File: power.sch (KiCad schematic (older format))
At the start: 5 parts, among them U301 MCP1754ST-3302E/MB

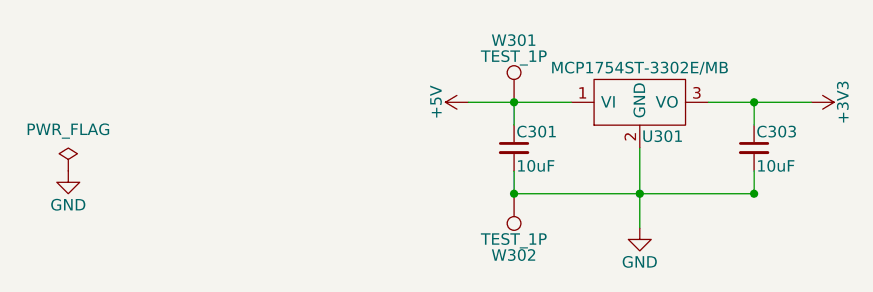
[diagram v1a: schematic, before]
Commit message: Add Fit, Manufacturer, MPN fields
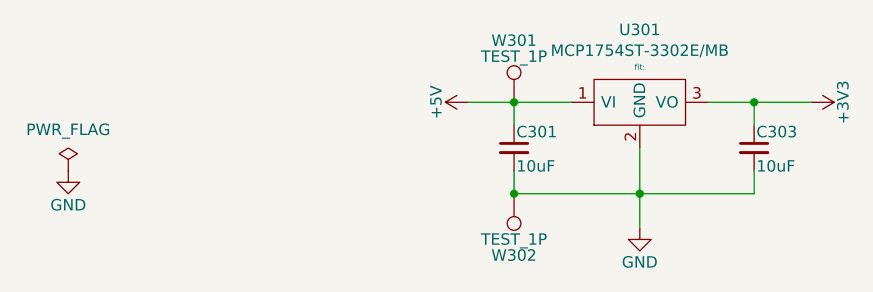
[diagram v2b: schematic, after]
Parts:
- C301, C303, W301, W302: Fit (none) -> fit:
- U301: Fit (none) -> fit:; MPN (none) -> MCP1754ST-3302E/MB; Manufacturer (none) -> Microchip
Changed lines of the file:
@@
 U 1 1 56F609E7
 P 5650 3750
-F 0 "U301" H 5750 3600 50  0000 C CNN
-F 1 "MCP1754ST-3302E/MB" H 5650 3900 50  0000 C CNN
+F 0 "U301" H 5650 4067 50  0000 C CNN
+F 1 "MCP1754ST-3302E/MB" H 5650 3976 50  0000 C CNN
 F 2 "TO_SOT_Packages_SMD:SOT89-3_Housing" H 5650 3750 50  0001 C CNN
 F 3 "" H 5650 3750 50  0000 C CNN
+F 4 "Microchip" H 5650 3750 50  0001 C CNN "Manufacturer"
+F 5 "MCP1754ST-3302E/MB" H 5650 3750 50  0001 C CNN "MPN"
+F 6 "fit: " H 5650 3904 25  0000 C CNN "Fit"
 	1    5650 3750
 	1    0    0    -1
@@
 F 2 "Capacitors_SMD:C_0805" H 5100 3950 50  0001 C CNN
 F 3 "" H 5100 3950 50  0000 C CNN
+F 4 "fit: " H 5100 3950 50  0001 C CNN "Fit"
 	1    5100 3950
 	1    0    0    -1
@@
 F 2 "Capacitors_SMD:C_0805" H 6150 3950 50  0001 C CNN
 F 3 "" H 6150 3950 50  0000 C CNN
+F 4 "fit: " H 6150 3950 50  0001 C CNN "Fit"
 	1    6150 3950
 	1    0    0    -1
@@
 Wire Wire Line
 	6150 4150 6150 4050
-Connection ~ 6150 4150
 Wire Wire Line
-	4900 3750 5350 3750
+	4900 3750 5100 3750
 Wire Wire Line
 	5100 3850 5100 3750
@@
 	5100 4050 5100 4150
 Wire Wire Line
-	5100 4150 6150 4150
+	5100 4150 5650 4150
 Wire Wire Line
-	5950 3750 6400 3750
+	5950 3750 6150 3750
 Connection ~ 6150 3750
 $Comp
@@
 F 2 "Measurement_Points:Measurement_Point_Round-SMD-Pad_Big" H 5300 3750 50  0001 C CNN
 F 3 "" H 5300 3750 50  0000 C CNN
+F 4 "fit: " H 5100 3750 50  0001 C CNN "Fit"
 	1    5100 3750
 	1    0    0    -1
@@
 F 2 "Measurement_Points:Measurement_Point_Round-SMD-Pad_Big" H 5300 4150 50  0001 C CNN
 F 3 "" H 5300 4150 50  0000 C CNN
+F 4 "fit: " H 5100 4150 50  0001 C CNN "Fit"
 	1    5100 4150
 	-1   0    0    1
 $EndComp
 Wire Wire Line
-	5650 3950 5650 4300
+	5650 3950 5650 4150
 Connection ~ 5100 4150
 $Comp
@@
 	1    0    0    -1
 $EndComp
+Wire Wire Line
+	5650 4150 6150 4150
+Wire Wire Line
+	5650 4150 5650 4300
+Wire Wire Line
+	5100 3750 5350 3750
+Wire Wire Line
+	6150 3750 6400 3750
 $EndSCHEMATC

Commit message: Add Cap voltage rating, Put PCB ref on cupper, add note for variants
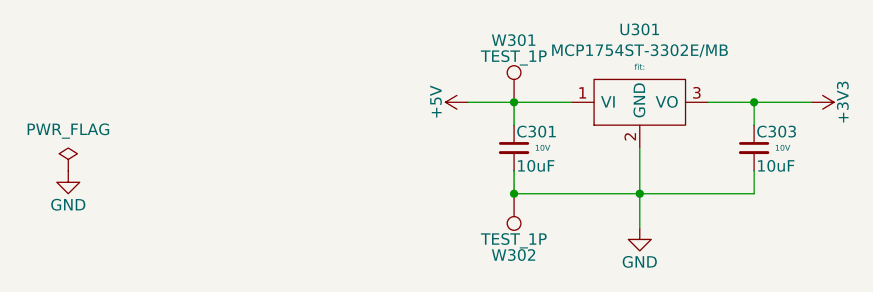
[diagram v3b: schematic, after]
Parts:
- C301, C303: CapRatedVoltage (none) -> 10V
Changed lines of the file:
@@
 F 3 "" H 5100 3950 50  0000 C CNN
 F 4 "fit: " H 5100 3950 50  0001 C CNN "Fit"
+F 5 "10V" H 5225 3950 25  0000 C CNN "CapRatedVoltage"
 	1    5100 3950
 	1    0    0    -1
@@
 F 3 "" H 6150 3950 50  0000 C CNN
 F 4 "fit: " H 6150 3950 50  0001 C CNN "Fit"
+F 5 "10V" H 6275 3950 25  0000 C CNN "CapRatedVoltage"
 	1    6150 3950
 	1    0    0    -1
